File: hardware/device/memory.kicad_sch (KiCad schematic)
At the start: 1 part, among them J3 Micro_SD_Card_Det_Hirose_DM3AT

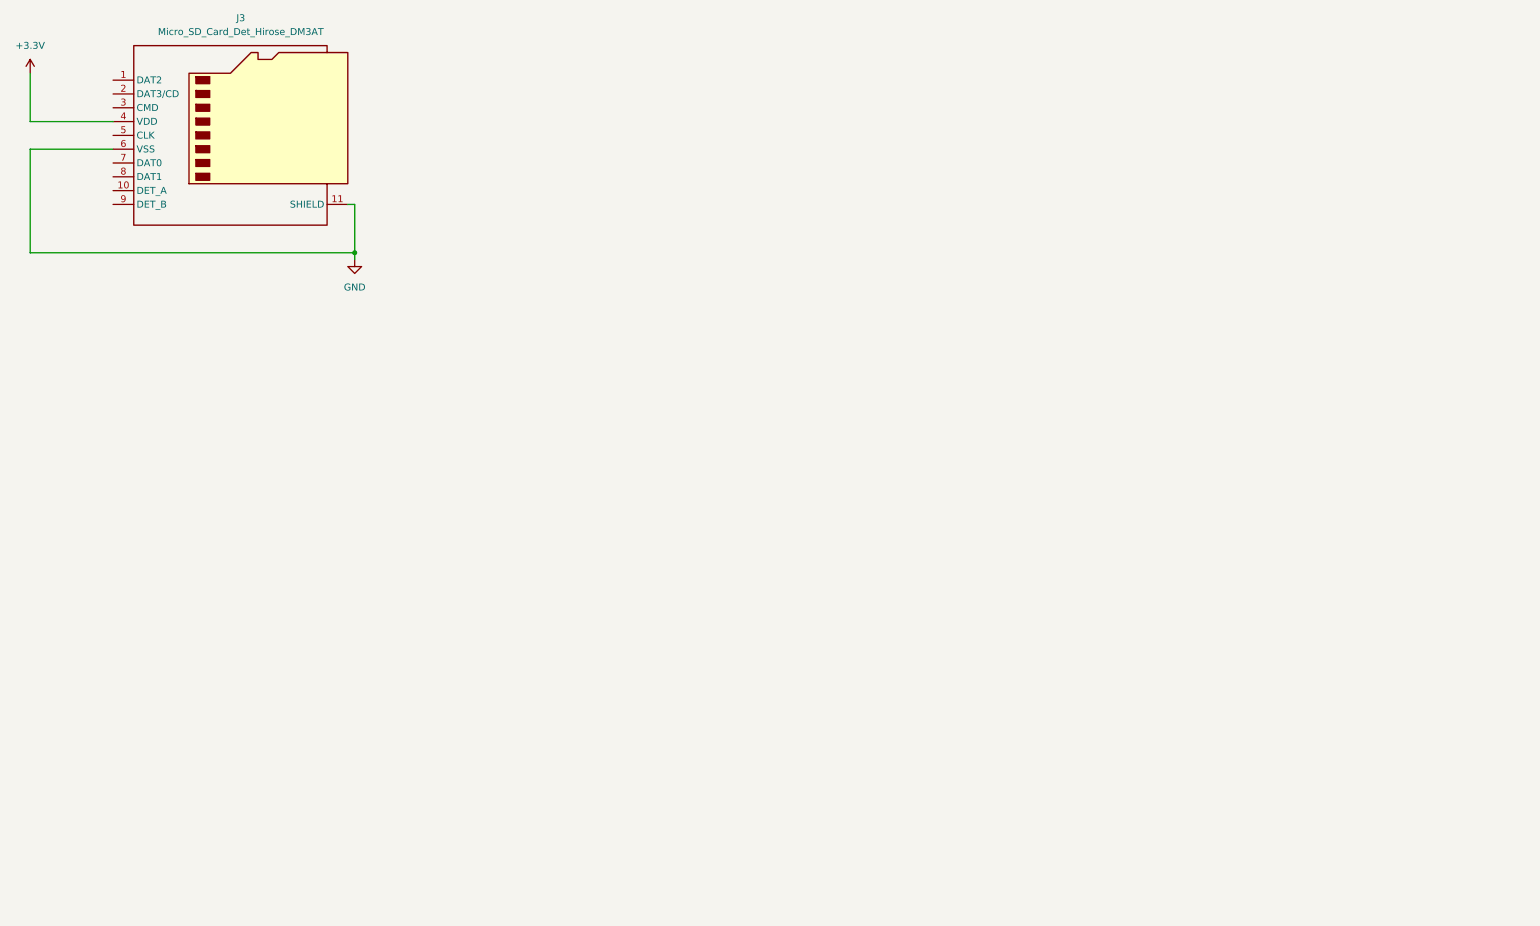
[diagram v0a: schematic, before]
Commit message: feat: various footprint updates, 3d models, tollerances
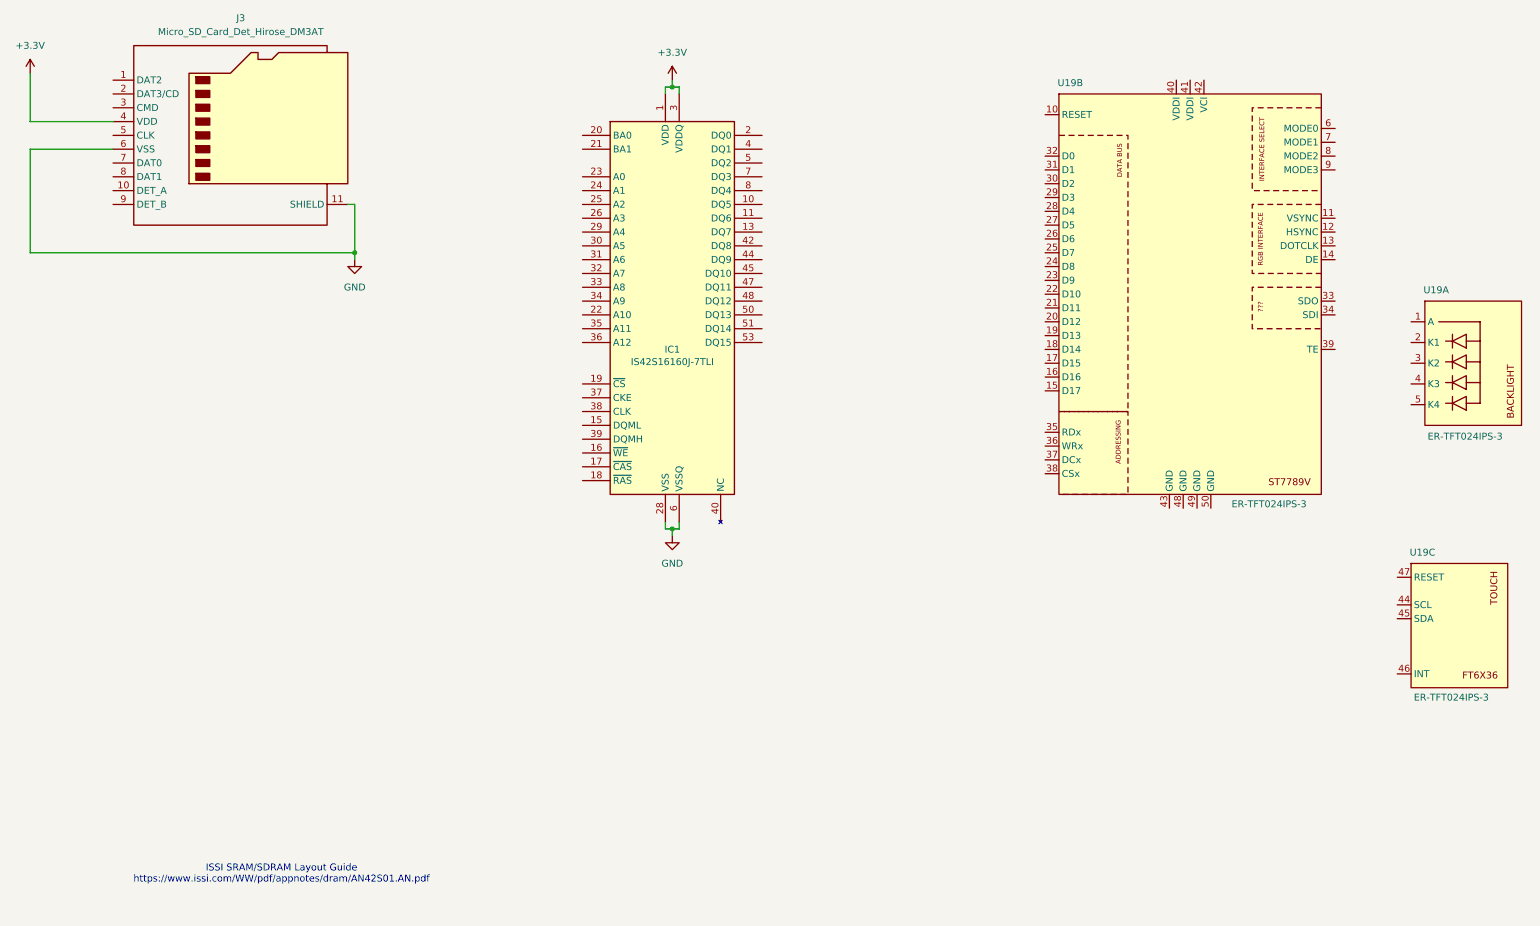
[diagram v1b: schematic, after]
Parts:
- added IC1: IS42S16160J-7TLI, pocket_synth:SOP80P1176X120-54N, symbol pocket_synth:IS42S16160J-7TLI
- added U19: ER-TFT024IPS-3, pocket_synth:ER-TFT024IPS-3, symbol pocket_synth:ER-TFT024IPS-3
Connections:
- net +3.3V: now also IC1.1 (VDD), IC1.14 (VDD), IC1.27 (VDD), IC1.3 (VDDQ), IC1.43 (VDDQ), IC1.49 (VDDQ), IC1.9 (VDDQ)
- net GND: now also IC1.12 (VSSQ), IC1.28 (VSS), IC1.41 (VSS), IC1.46 (VSSQ), IC1.52 (VSSQ), IC1.54 (VSS), IC1.6 (VSSQ)
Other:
- note added: "ISSI SRAM/SDRAM Layout Guide https://www.issi.com/WW/pdf/appnotes/dram/AN42S01.AN.pdf"

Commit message: feat: audio schematic, FMC bus, SDRAM connections
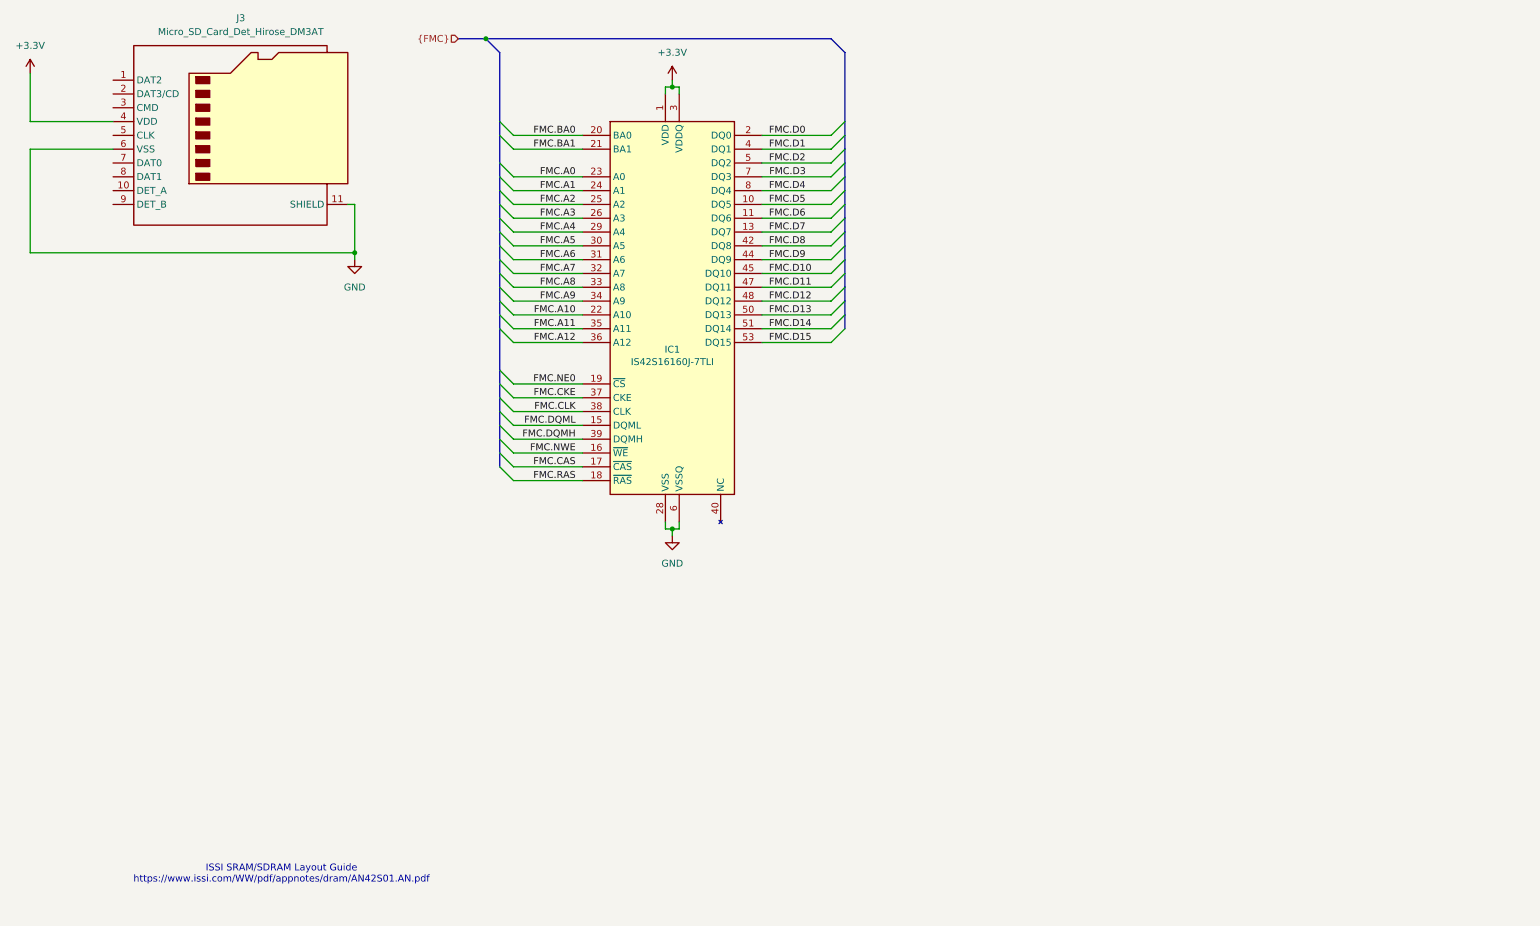
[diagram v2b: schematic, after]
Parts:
- removed U19: ER-TFT024IPS-3, pocket_synth:ER-TFT024IPS-3, symbol pocket_synth:ER-TFT024IPS-3
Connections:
- net FMC.D5: now reaches IC1.10 (DQ5)
- net FMC.D6: now reaches IC1.11 (DQ6)
- net FMC.D7: now reaches IC1.13 (DQ7)
- net FMC.DQML: now reaches IC1.15 (DQML)
- net FMC.NWE: now reaches IC1.16 (~{WE})
- net FMC.CAS: now reaches IC1.17 (~{CAS})
- net FMC.RAS: now reaches IC1.18 (~{RAS})
- net FMC.NE0: now reaches IC1.19 (~{CS})
- net FMC.D0: now reaches IC1.2 (DQ0)
- net FMC.BA0: now reaches IC1.20 (BA0)
- net FMC.BA1: now reaches IC1.21 (BA1)
- net FMC.A10: now reaches IC1.22 (A10)
- net FMC.A0: now reaches IC1.23 (A0)
- net FMC.A1: now reaches IC1.24 (A1)
- net FMC.A2: now reaches IC1.25 (A2)
- net FMC.A3: now reaches IC1.26 (A3)
- net FMC.A4: now reaches IC1.29 (A4)
- net FMC.A5: now reaches IC1.30 (A5)
- net FMC.A6: now reaches IC1.31 (A6)
- net FMC.A7: now reaches IC1.32 (A7)
- net FMC.A8: now reaches IC1.33 (A8)
- net FMC.A9: now reaches IC1.34 (A9)
- net FMC.A11: now reaches IC1.35 (A11)
- net FMC.A12: now reaches IC1.36 (A12)
- net FMC.CKE: now reaches IC1.37 (CKE)
- net FMC.CLK: now reaches IC1.38 (CLK)
- net FMC.DQMH: now reaches IC1.39 (DQMH)
- net FMC.D1: now reaches IC1.4 (DQ1)
- net FMC.D8: now reaches IC1.42 (DQ8)
- net FMC.D9: now reaches IC1.44 (DQ9)
- net FMC.D10: now reaches IC1.45 (DQ10)
- net FMC.D11: now reaches IC1.47 (DQ11)
- net FMC.D12: now reaches IC1.48 (DQ12)
- net FMC.D2: now reaches IC1.5 (DQ2)
- net FMC.D13: now reaches IC1.50 (DQ13)
- net FMC.D14: now reaches IC1.51 (DQ14)
- net FMC.D15: now reaches IC1.53 (DQ15)
- net FMC.D3: now reaches IC1.7 (DQ3)
- net FMC.D4: now reaches IC1.8 (DQ4)

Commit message: feat: various layouts, changed SDRAM to BGA
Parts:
- removed IC1: IS42S16160J-7TLI, pocket_synth:SOP80P1176X120-54N, symbol pocket_synth:IS42S16160J-7TLI
- added IC2: IS42S16160J-7BLI, pocket_synth:IS42S16160J-7BLI, symbol pocket_synth:IS42S16160J-7BLI
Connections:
- net +3.3V: now also IC2.A7 (VDDQ), IC2.A9 (VDD), IC2.B3 (VDDQ), IC2.C7 (VDDQ), IC2.D3 (VDDQ), IC2.E7 (VDD), IC2.J9 (VDD)
- net FMC.A0: now also IC2.H7 (A0)
- net FMC.A1: now also IC2.H8 (A1)
- net FMC.A10: now also IC2.H9 (A10)
- net FMC.A11: now also IC2.G2 (A11)
- net FMC.A12: now also IC2.G1 (A12)
- net FMC.A2: now also IC2.J8 (A2)
- net FMC.A3: now also IC2.J7 (A3)
- net FMC.A4: now also IC2.J3 (A4)
- net FMC.A5: now also IC2.J2 (A5)
- net FMC.A6: now also IC2.H3 (A6)
- net FMC.A7: now also IC2.H2 (A7)
- net FMC.A8: now also IC2.H1 (A8)
- net FMC.A9: now also IC2.G3 (A9)
- net FMC.BA0: now also IC2.G7 (BA0)
- net FMC.BA1: now also IC2.G8 (BA1)
- net FMC.CAS: now also IC2.F7 (~{CAS})
- net FMC.CKE: now also IC2.F3 (CKE)
- net FMC.CLK: now also IC2.F2 (CLK)
- net FMC.D0: now also IC2.A8 (DQ0)
- net FMC.D1: now also IC2.B9 (DQ1)
- net FMC.D10: now also IC2.D1 (DQ10)
- net FMC.D11: now also IC2.C2 (DQ11)
- net FMC.D12: now also IC2.C1 (DQ12)
- net FMC.D13: now also IC2.B2 (DQ13)
- net FMC.D14: now also IC2.B1 (DQ14)
- net FMC.D15: now also IC2.A2 (DQ15)
- net FMC.D2: now also IC2.B8 (DQ2)
- net FMC.D3: now also IC2.C9 (DQ3)
- net FMC.D4: now also IC2.C8 (DQ4)
- net FMC.D5: now also IC2.D9 (DQ5)
- net FMC.D6: now also IC2.D8 (DQ6)
- net FMC.D7: now also IC2.E9 (DQ7)
- net FMC.D8: now also IC2.E1 (DQ8)
- net FMC.D9: now also IC2.D2 (DQ9)
- net FMC.DQMH: now also IC2.F1 (DQMH)
- net FMC.DQML: now also IC2.E8 (DQML)
- net FMC.NE0: now also IC2.G9 (~{CS})
- net FMC.NWE: now also IC2.F9 (~{WE})
- net FMC.RAS: now also IC2.F8 (~{RAS})
- net GND: now also IC2.A1 (VSS), IC2.A3 (VSSQ), IC2.B7 (VSSQ), IC2.C3 (VSSQ), IC2.D7 (VSSQ), IC2.E3 (VSS), IC2.J1 (VSS)
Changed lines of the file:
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@@
 	)
 	(symbol
-		(lib_id "pocket_synth:IS42S16160J-7TLI")
+		(lib_id "pocket_synth:IS42S16160J-7BLI")
 		(at 139.7 73.66 0)
 		(unit 1)
@@
 		(on_board yes)
 		(dnp no)
-		(property "Reference" "IC1"
-			(at 139.7 81.28 0)
-			(effects
-				(font
-					(size 1.27 1.27)
-				)
-			)
-		)
-		(property "Value" "IS42S16160J-7TLI"
-			(at 139.7 83.566 0)
-			(effects
-				(font
-					(size 1.27 1.27)
-				)
-			)
-		)
-		(property "Footprint" "pocket_synth:SOP80P1176X120-54N"
-			(at 168.91 168.58 0)
-			(effects
-				(font
-					(size 1.27 1.27)
-				)
-				(justify left top)
-				(hide yes)
-			)
-		)
-		(property "Datasheet" "http://www.issi.com/WW/pdf/42-45S83200J-16160J.pdf"
-			(at 168.91 268.58 0)
-			(effects
-				(font
-					(size 1.27 1.27)
-				)
-				(justify left top)
-				(hide yes)
-			)
-		)
-		(property "Description" "DRAM 256M, 3.3V, SDRAM 16Mx16 143MHz"
-			(at 139.7 73.66 0)
+		(property "Reference" "IC2"
+			(at 139.7 81.534 0)
+			(effects
+				(font
+					(size 1.27 1.27)
+				)
+			)
+		)
+		(property "Value" "IS42S16160J-7BLI"
+			(at 139.7 84.074 0)
+			(effects
+				(font
+					(size 1.27 1.27)
+				)
+			)
+		)
+		(property "Footprint" "pocket_synth:IS42S16160J-7BLI"
+			(at 152.4 135.56 0)
+			(effects
+				(font
+					(size 1.27 1.27)
+				)
+				(justify left top)
+				(hide yes)
+			)
+		)
+		(property "Datasheet" "https://www.mouser.ca/datasheet/2/198/42_45S83200J_16160J-462626.pdf"
+			(at 152.4 235.56 0)
+			(effects
+				(font
+					(size 1.27 1.27)
+				)
+				(justify left top)
+				(hide yes)
+			)
+		)
+		(property "Description" "DRAM 256M, 3.3V, SDRAM, 16Mx16, 143Mhz, 54 ball BGA (8mmx8mm) RoHS, IT"
+			(at 123.19 40.64 0)
 			(effects
 				(font
@@
 		)
 		(property "Height" "1.2"
-			(at 168.91 468.58 0)
-			(effects
-				(font
-					(size 1.27 1.27)
-				)
-				(justify left top)
-				(hide yes)
-			)
-		)
-		(property "Mouser Part Number" "870-IS42S16160J-7TLI"
-			(at 168.91 568.58 0)
-			(effects
-				(font
-					(size 1.27 1.27)
-				)
-				(justify left top)
-				(hide yes)
-			)
-		)
-		(property "Mouser Price/Stock" "https://www.mouser.co.uk/ProductDetail/ISSI/IS42S16160J-7TLI?qs=uCnMRCNammmen%252BmWnq1g5A%3D%3D"
-			(at 168.91 668.58 0)
+			(at 152.4 435.56 0)
+			(effects
+				(font
+					(size 1.27 1.27)
+				)
+				(justify left top)
+				(hide yes)
+			)
+		)
+		(property "Mouser Part Number" "870-42S16160J7BLI"
+			(at 152.4 535.56 0)
+			(effects
+				(font
+					(size 1.27 1.27)
+				)
+				(justify left top)
+				(hide yes)
+			)
+		)
+		(property "Mouser Price/Stock" "https://www.mouser.co.uk/ProductDetail/ISSI/IS42S16160J-7BLI?qs=bHq4TaS7gBfDC8kKmlCy6g%3D%3D"
+			(at 152.4 635.56 0)
 			(effects
 				(font
@@
 		)
 		(property "Manufacturer_Name" "Integrated Silicon Solution Inc."
-			(at 168.91 768.58 0)
-			(effects
-				(font
-					(size 1.27 1.27)
-				)
-				(justify left top)
-				(hide yes)
-			)
-		)
-		(property "Manufacturer_Part_Number" "IS42S16160J-7TLI"
-			(at 168.91 868.58 0)
-			(effects
-				(font
-					(size 1.27 1.27)
-				)
-				(justify left top)
-				(hide yes)
-			)
-		)
-		(pin "41"
-		)
-		(pin "40"
-		)
-		(pin "39"
-		)
-		(pin "38"
-		)
-		(pin "37"
-		)
-		(pin "36"
-		)
-		(pin "35"
-		)
-		(pin "34"
-		)
-		(pin "33"
-		)
-		(pin "32"
-		)
-		(pin "31"
-		)
-		(pin "30"
-		)
-		(pin "29"
-		)
-		(pin "28"
-		)
-		(pin "1"
-		)
-		(pin "22"
-		)
-		(pin "4"
-		)
-		(pin "14"
-		)
-		(pin "6"
-		)
-		(pin "16"
-		)
-		(pin "19"
-		)
-		(pin "48"
-		)
-		(pin "47"
-		)
-		(pin "46"
-		)
-		(pin "45"
-		)
-		(pin "2"
-		)
-		(pin "44"
-		)
-		(pin "43"
-		)
-		(pin "42"
-		)
-		(pin "3"
-		)
-		(pin "10"
-		)
-		(pin "15"
-		)
-		(pin "5"
-		)
-		(pin "25"
-		)
-		(pin "7"
-		)
-		(pin "12"
-		)
-		(pin "18"
-		)
-		(pin "17"
-		)
-		(pin "8"
-		)
-		(pin "9"
-		)
-		(pin "11"
-		)
-		(pin "21"
-		)
-		(pin "20"
-		)
-		(pin "54"
-		)
-		(pin "49"
-		)
-		(pin "51"
-		)
-		(pin "27"
-		)
-		(pin "24"
-		)
-		(pin "26"
-		)
-		(pin "13"
-		)
-		(pin "23"
-		)
-		(pin "52"
-		)
-		(pin "50"
-		)
-		(pin "53"
+			(at 152.4 735.56 0)
+			(effects
+				(font
+					(size 1.27 1.27)
+				)
+				(justify left top)
+				(hide yes)
+			)
+		)
+		(property "Manufacturer_Part_Number" "IS42S16160J-7BLI"
+			(at 152.4 835.56 0)
+			(effects
+				(font
+					(size 1.27 1.27)
+				)
+				(justify left top)
+				(hide yes)
+			)
+		)
+		(pin "E7"
+		)
+		(pin "A8"
+		)
+		(pin "D7"
+		)
+		(pin "G1"
+		)
+		(pin "G7"
+		)
+		(pin "F9"
+		)
+		(pin "C9"
+		)
+		(pin "C8"
+		)
+		(pin "C2"
+		)
+		(pin "C1"
+		)
+		(pin "B2"
+		)
+		(pin "B1"
+		)
+		(pin "A2"
+		)
+		(pin "H1"
+		)
+		(pin "E1"
+		)
+		(pin "D2"
+		)
+		(pin "D1"
+		)
+		(pin "H2"
+		)
+		(pin "D9"
+		)
+		(pin "D8"
+		)
+		(pin "E9"
+		)
+		(pin "J8"
+		)
+		(pin "G2"
+		)
+		(pin "H9"
+		)
+		(pin "F3"
+		)
+		(pin "B7"
+		)
+		(pin "B9"
+		)
+		(pin "D3"
+		)
+		(pin "J7"
+		)
+		(pin "E3"
+		)
+		(pin "H7"
+		)
+		(pin "F2"
+		)
+		(pin "J1"
+		)
+		(pin "J2"
+		)
+		(pin "A9"
+		)
+		(pin "E2"
+		)
+		(pin "H8"
+		)
+		(pin "H3"
+		)
+		(pin "A3"
+		)
+		(pin "A1"
+		)
+		(pin "F1"
+		)
+		(pin "C3"
+		)
+		(pin "J9"
+		)
+		(pin "E8"
+		)
+		(pin "B3"
+		)
+		(pin "F7"
+		)
+		(pin "A7"
+		)
+		(pin "F8"
+		)
+		(pin "G8"
+		)
+		(pin "C7"
+		)
+		(pin "G3"
+		)
+		(pin "G9"
+		)
+		(pin "J3"
+		)
+		(pin "B8"
 		)
 		(instances
 			(project ""
 				(path "/485383b8-00f4-4405-b270-de249939cff4/d641c287-d179-45c1-92b5-f0a3902e6ffa"
-					(reference "IC1")
+					(reference "IC2")
 					(unit 1)
 				)
